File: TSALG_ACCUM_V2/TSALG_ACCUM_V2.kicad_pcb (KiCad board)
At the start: 2 copper layers, 140 x 60 mm, 99 parts, among them J1 Conn_01x02_Pin, J10 Conn_01x02_Pin, J2 Conn_01x02_Pin, J3 Conn_01x03_Pin, J4 Conn_01x02_Pin, J5 Conn_01x02_Pin, J6 Conn_01x02_Pin, J7 Conn_01x03_Pin, J8 Conn_01x02_Pin, J9 Conn_01x03_Pin, U1 TLV431, U10 LM393, U11 LM393, U12 LM393, U2 LTV-817S, U3 B1212, U4 LTV-847S, U5 uA7805, U6 TLV431, U7 MCP6002-xSN, U8 LM393, U9 LM393

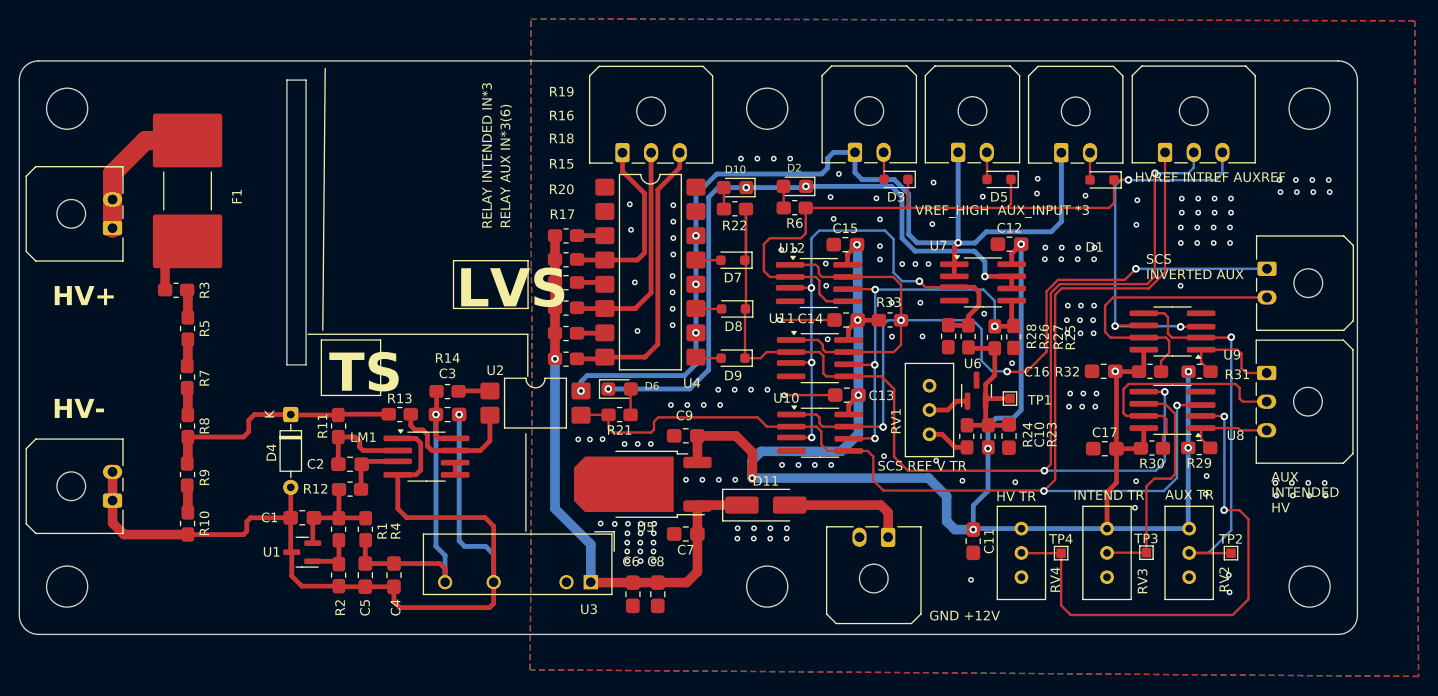
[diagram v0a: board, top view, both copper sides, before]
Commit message: ACCUM BOARDs BATCH ORDER
ts indicator
imd latch v2
tsalg accum v2.1
tsalg hvb v2.1
batch order
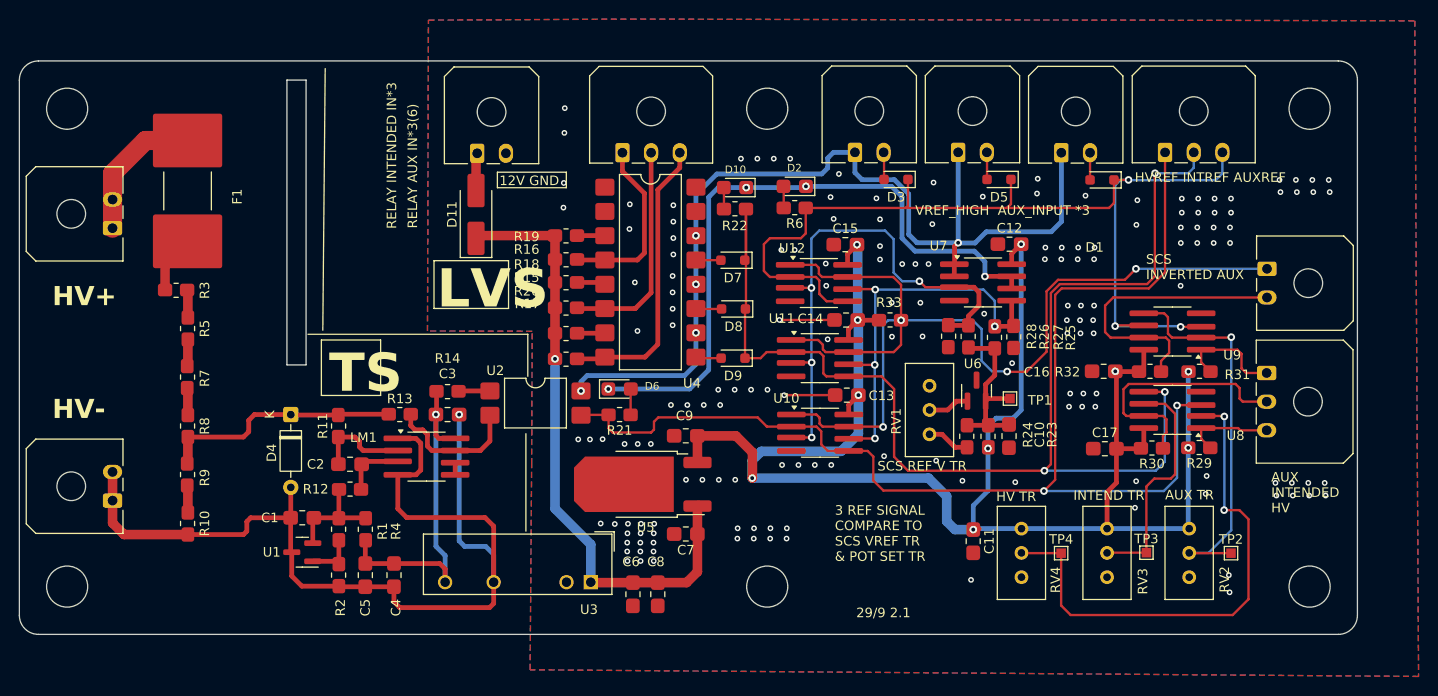
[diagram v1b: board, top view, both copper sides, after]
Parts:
- moved J10 58.8 mm to (125.9, 73.7), turned to 0 degrees
- moved D11 42.9 mm to (125.8, 80.1), turned to 90 degrees
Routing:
- net Net-(D11-A): track 13.2 -> 3.95 mm
- net GLV+: track 61.0 -> 64.9 mm
- net GLV-: vias 161 -> 165
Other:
- board text added: "12V GND"
- board text added: "29/9 2.1"
- board text added: "3 REF SIGNAL COMPARE TO SCS VREF TR & POT SET TR"
- board text removed: "GND +12V"
